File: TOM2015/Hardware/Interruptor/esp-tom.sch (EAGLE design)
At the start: 20 parts, among them K1 G5L, X1 MKDSN1,5/2-5,08, X2 MKDSN1,5/3-5,08

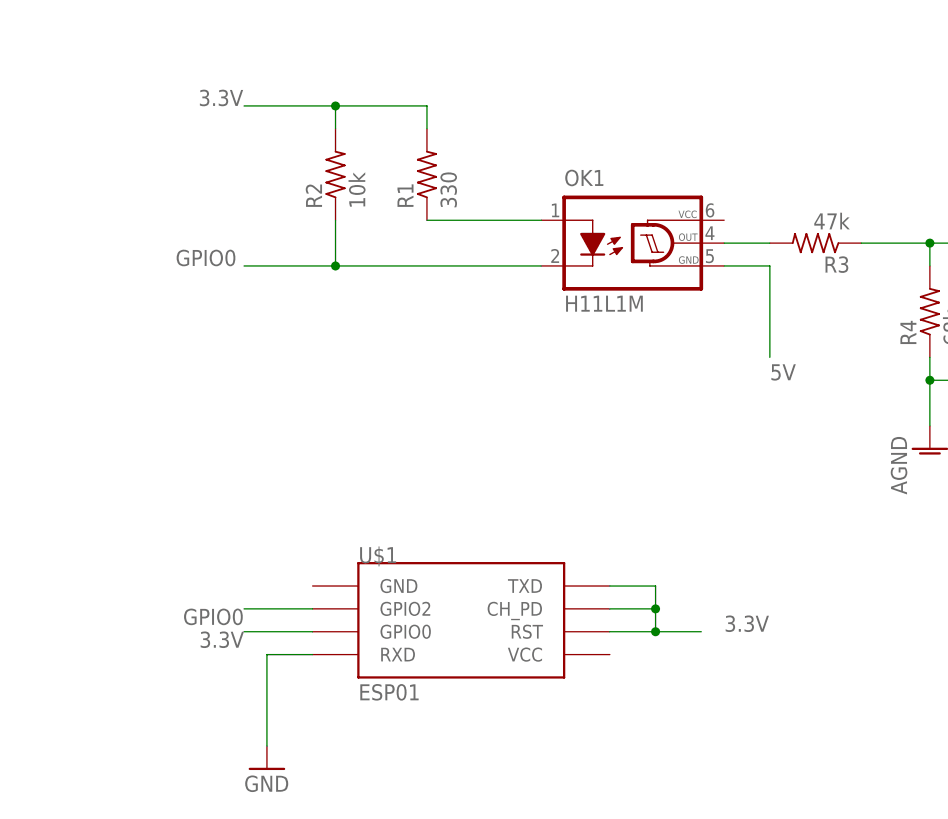
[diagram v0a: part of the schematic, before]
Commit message: Versão final do tom
Versão final do Tom com as ligações do esp corretas e o desenho correto
do componente TIL111
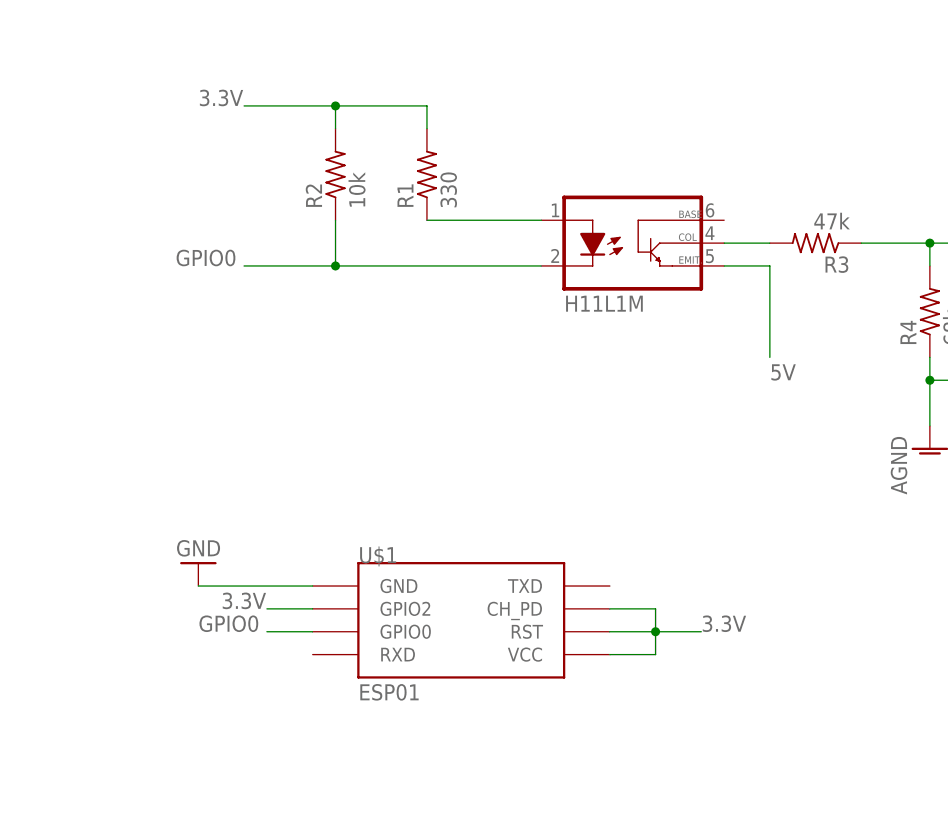
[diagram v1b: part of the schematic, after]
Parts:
- OK1: device optocoupler:H11L1M -> optocoupler2:H11L1M
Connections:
- net 3.3V: now also U$1.GPIO2, U$1.VCC; no longer U$1.GPIO0, U$1.TXD
- net GND: now also U$1.GND; no longer U$1.RXD
- net GPIO0: now also U$1.GPIO0; no longer U$1.GPIO2
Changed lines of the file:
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@@
 <part name="R1" library="resistor" deviceset="R-US_" device="0204/7" value="330"/>
 <part name="R2" library="resistor" deviceset="R-US_" device="0204/7" value="10k"/>
-<part name="OK1" library="optocoupler" deviceset="H11L*M" device="" technology="1"/>
+<part name="OK1" library="optocoupler2" deviceset="H11L*M" device="" technology="1"/>
 <part name="Q1" library="transistors" deviceset="2N700*" device="_TO92" technology="0"/>
 <part name="K1" library="relay" deviceset="G5L" device=""/>
@@
 <instance part="C1" gate="G$1" x="111.76" y="35.56"/>
 <instance part="D1" gate="1" x="114.3" y="68.58" rot="R90"/>
-<instance part="GND3" gate="1" x="27.94" y="-15.24"/>
+<instance part="GND3" gate="1" x="20.32" y="7.62" rot="R180"/>
 <instance part="X1" gate="-1" x="-53.34" y="96.52" rot="R180"/>
 <instance part="X1" gate="-2" x="-53.34" y="83.82" rot="R180"/>
@@
 </segment>
 <segment>
-<pinref part="U$1" gate="G$1" pin="CH_PD"/>
-<wire x1="71.12" y1="0" x2="71.12" y2="2.54" width="0.1524" layer="91"/>
-<wire x1="71.12" y1="2.54" x2="66.04" y2="2.54" width="0.1524" layer="91"/>
-<junction x="71.12" y="0"/>
-<wire x1="71.12" y1="0" x2="76.2" y2="0" width="0.1524" layer="91"/>
-<label x="78.74" y="0" size="1.778" layer="95"/>
-<pinref part="U$1" gate="G$1" pin="RST"/>
-<wire x1="71.12" y1="0" x2="66.04" y2="0" width="0.1524" layer="91"/>
-<pinref part="U$1" gate="G$1" pin="TXD"/>
-<wire x1="71.12" y1="2.54" x2="71.12" y2="5.08" width="0.1524" layer="91"/>
-<wire x1="71.12" y1="5.08" x2="66.04" y2="5.08" width="0.1524" layer="91"/>
-<junction x="71.12" y="2.54"/>
-</segment>
-<segment>
 <label x="127" y="121.92" size="1.778" layer="95"/>
 <pinref part="C3" gate="G$1" pin="+"/>
@@
 </segment>
 <segment>
-<pinref part="U$1" gate="G$1" pin="GPIO0"/>
-<wire x1="33.02" y1="0" x2="25.4" y2="0" width="0.1524" layer="91"/>
-<label x="25.4" y="0" size="1.778" layer="95" rot="R180"/>
+<pinref part="U$1" gate="G$1" pin="CH_PD"/>
+<wire x1="66.04" y1="2.54" x2="71.12" y2="2.54" width="0.1524" layer="91"/>
+<wire x1="71.12" y1="2.54" x2="71.12" y2="0" width="0.1524" layer="91"/>
+<pinref part="U$1" gate="G$1" pin="VCC"/>
+<wire x1="71.12" y1="0" x2="71.12" y2="-2.54" width="0.1524" layer="91"/>
+<wire x1="71.12" y1="-2.54" x2="66.04" y2="-2.54" width="0.1524" layer="91"/>
+<pinref part="U$1" gate="G$1" pin="RST"/>
+<wire x1="66.04" y1="0" x2="71.12" y2="0" width="0.1524" layer="91"/>
+<junction x="71.12" y="0"/>
+<wire x1="71.12" y1="0" x2="76.2" y2="0" width="0.1524" layer="91"/>
+<label x="76.2" y="0" size="1.778" layer="95"/>
+</segment>
+<segment>
+<pinref part="U$1" gate="G$1" pin="GPIO2"/>
+<wire x1="33.02" y1="2.54" x2="27.94" y2="2.54" width="0.1524" layer="91"/>
+<label x="22.86" y="2.54" size="1.778" layer="95"/>
 </segment>
 </net>
@@
 </segment>
 <segment>
-<pinref part="U$1" gate="G$1" pin="GPIO2"/>
-<wire x1="33.02" y1="2.54" x2="25.4" y2="2.54" width="0.1524" layer="91"/>
-<label x="25.4" y="2.54" size="1.778" layer="95" rot="R180"/>
+<pinref part="U$1" gate="G$1" pin="GPIO0"/>
+<wire x1="33.02" y1="0" x2="27.94" y2="0" width="0.1524" layer="91"/>
+<label x="20.32" y="0" size="1.778" layer="95"/>
 </segment>
 </net>
@@
 <net name="GND" class="0">
 <segment>
-<pinref part="GND3" gate="1" pin="GND"/>
-<wire x1="27.94" y1="-2.54" x2="27.94" y2="-12.7" width="0.1524" layer="91"/>
-<pinref part="U$1" gate="G$1" pin="RXD"/>
-<wire x1="27.94" y1="-2.54" x2="33.02" y2="-2.54" width="0.1524" layer="91"/>
-</segment>
-<segment>
 <pinref part="C3" gate="G$1" pin="-"/>
 <wire x1="93.98" y1="111.76" x2="93.98" y2="106.68" width="0.1524" layer="91"/>
@@
 <wire x1="93.98" y1="104.14" x2="93.98" y2="106.68" width="0.1524" layer="91"/>
 </segment>
+<segment>
+<pinref part="U$1" gate="G$1" pin="GND"/>
+<pinref part="GND3" gate="1" pin="GND"/>
+<wire x1="33.02" y1="5.08" x2="20.32" y2="5.08" width="0.1524" layer="91"/>
+</segment>
 </net>
